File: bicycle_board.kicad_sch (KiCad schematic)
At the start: 57 parts, among them J1 Micro_SD_Card, J10 USB_A, J12 Conn_01x04, J13 Conn_01x04, J2 USB_C_Receptacle_USB2.0_16P, J6 Conn_01x08, J7 Conn_01x05, J8 Conn_01x02, J9 Conn_01x06, Q1 Q_NMOS_GSD, Q2 Q_NMOS_GSD, Q3 Q_NMOS_GSD, Q4 Q_NMOS_GSD, Q5 Q_NMOS_GSD, U13 NS4168, U14 ESP32-C3-WROOM-02U, U15 CH32V203C8T6, U7 74HC595, Y1 12MHz, Y2 32.768kHz

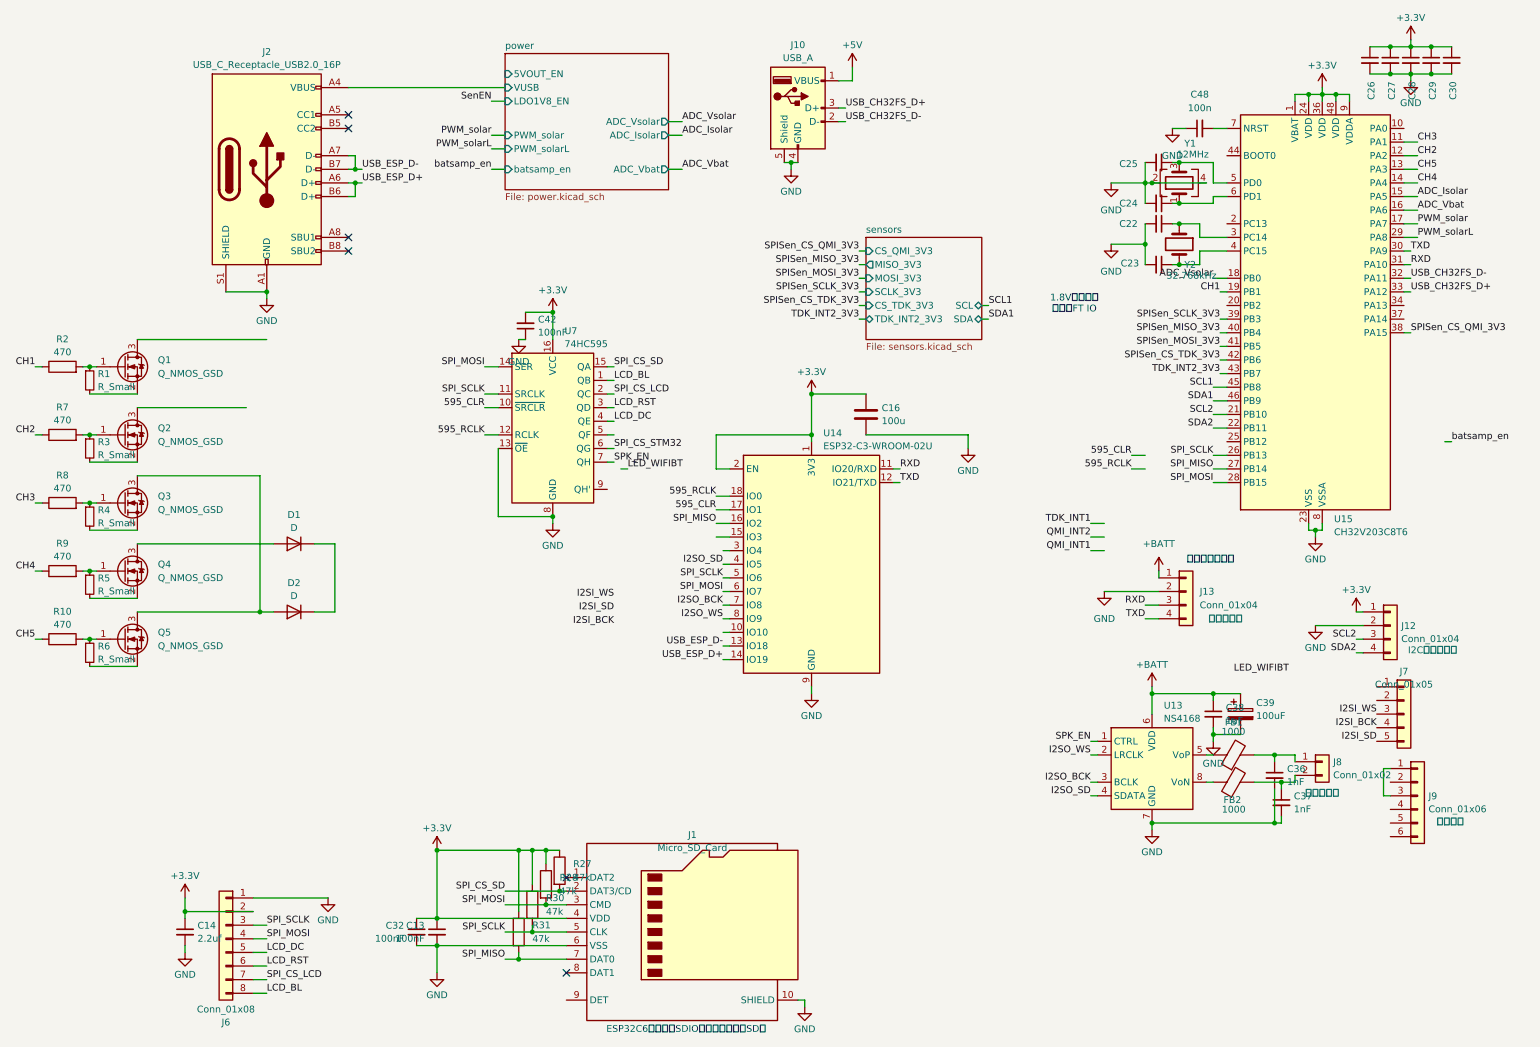
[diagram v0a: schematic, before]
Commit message: 修复一些DRC错误和警告，大多数信号接口改成SH1.0接口
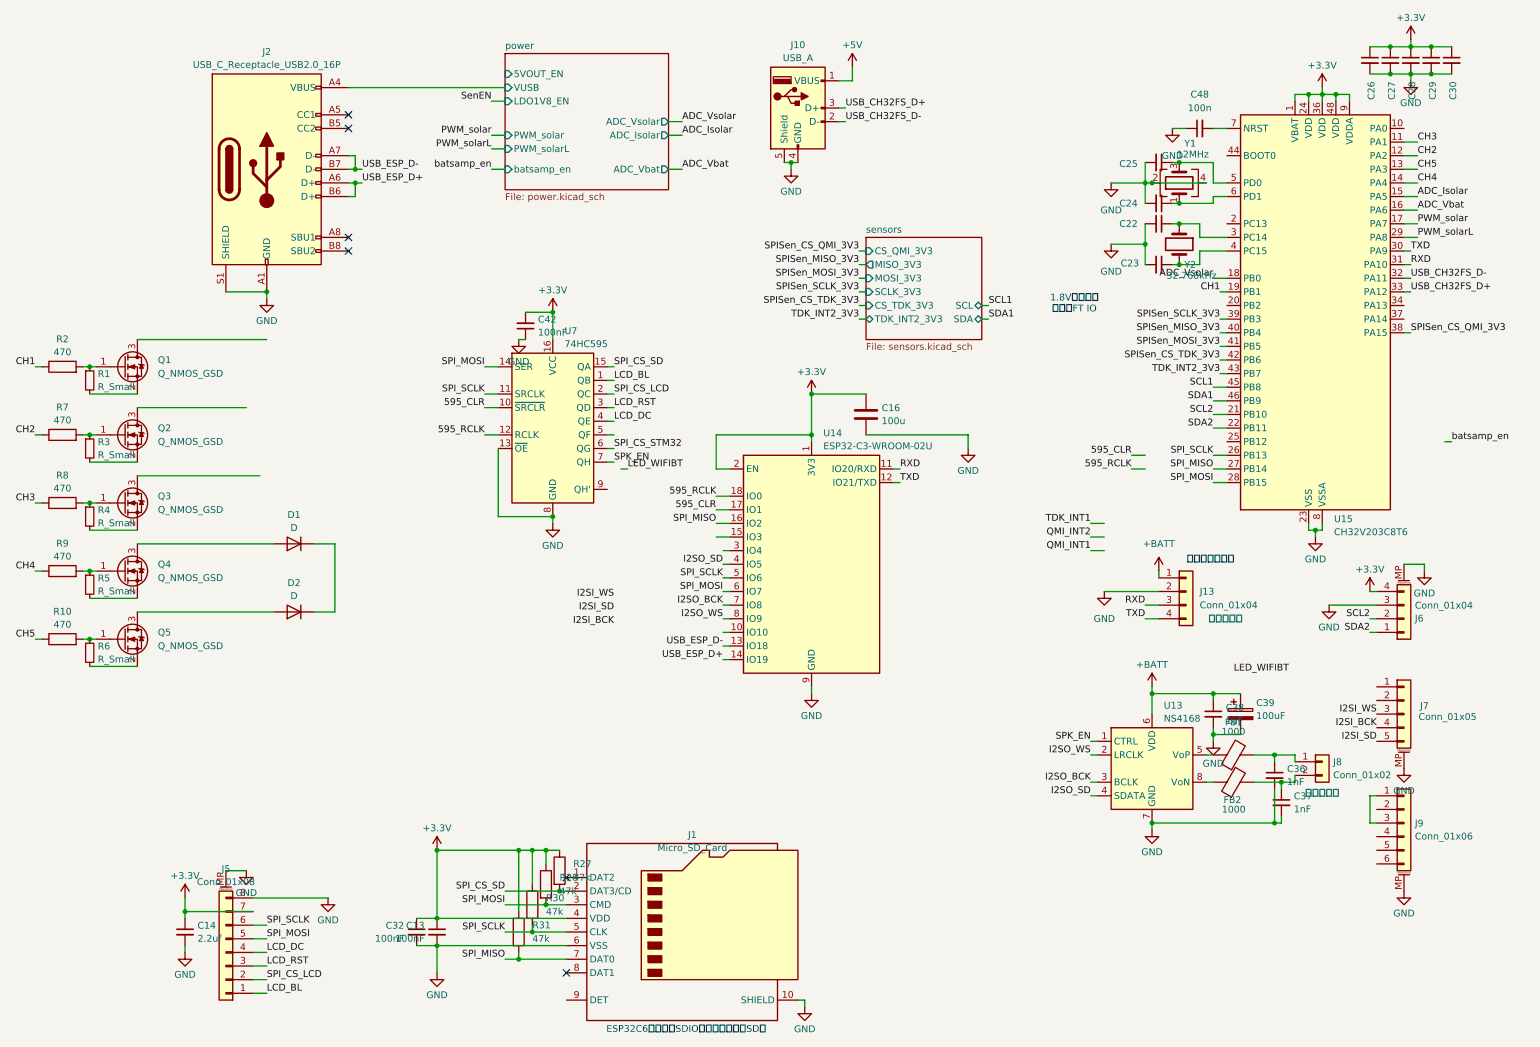
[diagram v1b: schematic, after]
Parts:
- removed J12: Conn_01x04, Connector_JST:JST_GH_BM04B-GHS-TBT_1x04-1MP_P1.25mm_Vertical, symbol Connector_Generic:Conn_01x04
- removed J6: Conn_01x08, Connector_JST:JST_GH_BM08B-GHS-TBT_1x08-1MP_P1.25mm_Vertical, symbol Connector_Generic:Conn_01x08
- added J5: Conn_01x08, Connector_JST:JST_SH_SM08B-SRSS-TB_1x08-1MP_P1.00mm_Horizontal, symbol Connector_Generic_MountingPin:Conn_01x08_MountingPin
- added J6: Conn_01x04, Connector_JST:JST_SH_SM04B-SRSS-TB_1x04-1MP_P1.00mm_Horizontal, symbol Connector_Generic_MountingPin:Conn_01x04_MountingPin
- J7: footprint Connector_JST:JST_GH_BM05B-GHS-TBT_1x05-1MP_P1.25mm_Vertical -> Connector_JST:JST_SH_SM05B-SRSS-TB_1x05-1MP_P1.00mm_Horizontal; symbol Connector_Generic:Conn_01x05 -> Connector_Generic_MountingPin:Conn_01x05_MountingPin
- J9: footprint Connector_JST:JST_SHL_SM06B-SHLS-TF_1x06-1MP_P1.00mm_Horizontal -> Connector_JST:JST_SH_SM06B-SRSS-TB_1x06-1MP_P1.00mm_Horizontal; symbol Connector_Generic:Conn_01x06 -> Connector_Generic_MountingPin:Conn_01x06_MountingPin
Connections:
- net +3.3V: now also J5.7 (Pin_7), J6.4 (Pin_4)
- net GND: now also J7.MP (MountPin), J9.MP (MountPin), J5.8 (Pin_8), J5.MP (MountPin), J6.3 (Pin_3), J6.MP (MountPin)
- net LCD_BL: now also J5.1 (Pin_1)
- net LCD_DC: now also J5.4 (Pin_4)
- net LCD_RST: now also J5.3 (Pin_3)
- net SCL2: now also J6.2 (Pin_2)
- net SDA2: now also J6.1 (Pin_1)
- net SPI_CS_LCD: now also J5.2 (Pin_2)
- net SPI_MOSI: now also J5.5 (Pin_5)
- net SPI_SCLK: now also J5.6 (Pin_6)
- net at D2.2 (A), Q5.3 (D): no longer Q3.3 (D)

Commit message: 添加霍尔元件接口，移除CH2,CH3 MOS通道，调整和连接布线，取消STM32与ESP32的SPI连接
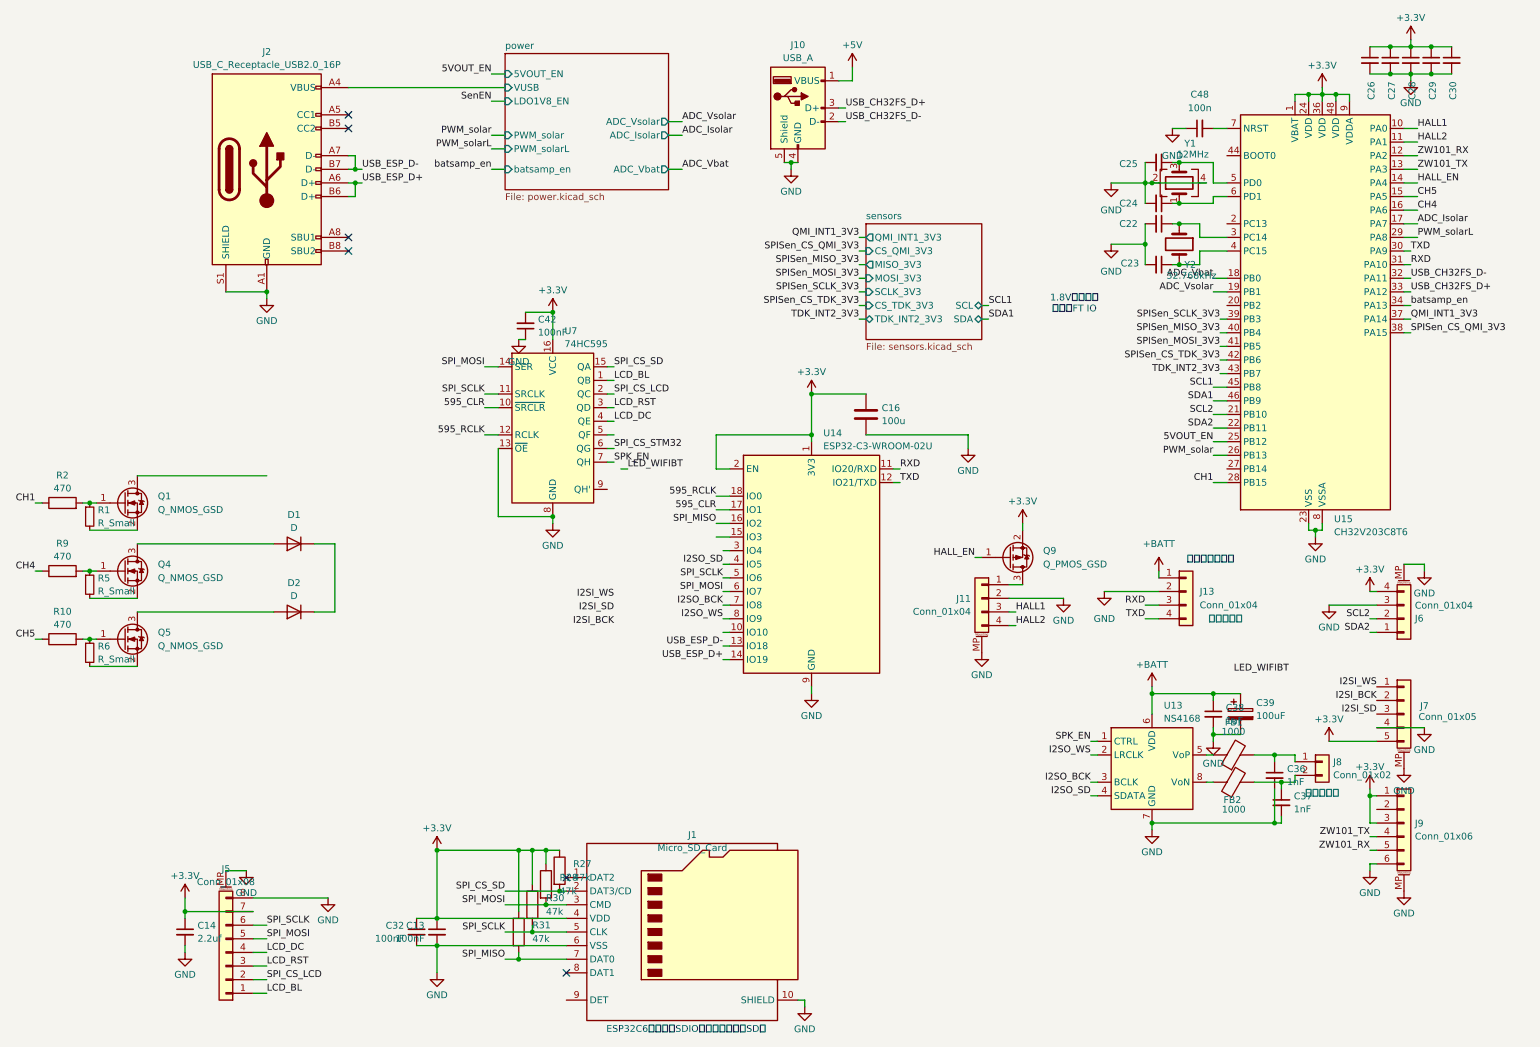
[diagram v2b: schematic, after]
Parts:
- removed Q2, Q3: Q_NMOS_GSD, Package_TO_SOT_SMD:SOT-23, symbol Device:Q_NMOS_GSD
- removed R3, R4: R_Small, Resistor_SMD:R_0402_1005Metric, symbol Device:R_Small
- removed R7, R8: 470, Resistor_SMD:R_0402_1005Metric, symbol Device:R
- added J11: Conn_01x04, Connector_JST:JST_SH_SM04B-SRSS-TB_1x04-1MP_P1.00mm_Horizontal, symbol Connector_Generic_MountingPin:Conn_01x04_MountingPin
- added Q9: Q_PMOS_GSD, Package_TO_SOT_SMD:SOT-523, symbol Device:Q_PMOS_GSD
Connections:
- net CH2 is gone; now on net ZW101_RX: U15.12 (PA2)
- net +3.3V: now also J7.5 (Pin_5), J9.1 (Pin_1), J9.3 (Pin_3), Q9.2 (S)
- net ADC_Isolar: now also U15.17 (PA7); no longer U15.15 (PA5)
- net ADC_Vbat: now also U15.18 (PB0); no longer U15.16 (PA6)
- net ADC_Vsolar: now also U15.19 (PB1); no longer U15.18 (PB0)
- net CH1: now also U15.28 (PB15); no longer U15.19 (PB1)
- net CH4: now also U15.16 (PA6); no longer U15.14 (PA4)
- net CH5: now also U15.15 (PA5); no longer U15.13 (PA3)
- net GND: now also J7.4 (Pin_4), J9.6 (Pin_6), J11.2 (Pin_2), J11.MP (MountPin)
- net I2SI_BCK: now also J7.2 (Pin_2); no longer J7.4 (Pin_4)
- net I2SI_SD: now also J7.3 (Pin_3); no longer J7.5 (Pin_5)
- net I2SI_WS: now also J7.1 (Pin_1); no longer J7.3 (Pin_3)
- net PWM_solar: now also U15.26 (PB13); no longer U15.17 (PA7)
- net SPI_MISO: no longer U15.27 (PB14)
- net SPI_MOSI: no longer U15.28 (PB15)
- net SPI_SCLK: no longer U15.26 (PB13)
- net batsamp_en: now also U15.34 (PA13)
- net HALL1: now reaches U15.10 (PA0)
- net HALL1: now also J11.3 (Pin_3)
- net 5VOUT_EN: now reaches U15.25 (PB12)
- net QMI_INT1_3V3: now reaches U15.37 (PA14)
- net ZW101_TX: now reaches J9.4 (Pin_4)
- net ZW101_TX: now also U15.13 (PA3)
- net ZW101_RX: now reaches J9.5 (Pin_5)
- net CH3 renamed HALL2
- net HALL2: now also J11.4 (Pin_4)
- new net: J11.1 (Pin_1), Q9.3 (D)
- new net HALL_EN: Q9.1 (G), U15.14 (PA4)
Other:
- sheet sensors ports: added QMI_INT1_3V3; removed none
- moved on the sheet: Q1, R1, R2

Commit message: 调整STM32 GPIO使用，移除右侧MOS通道，只在左侧底部保留2个，计划采用PCA9555/TCA9555 GPIO扩展芯片
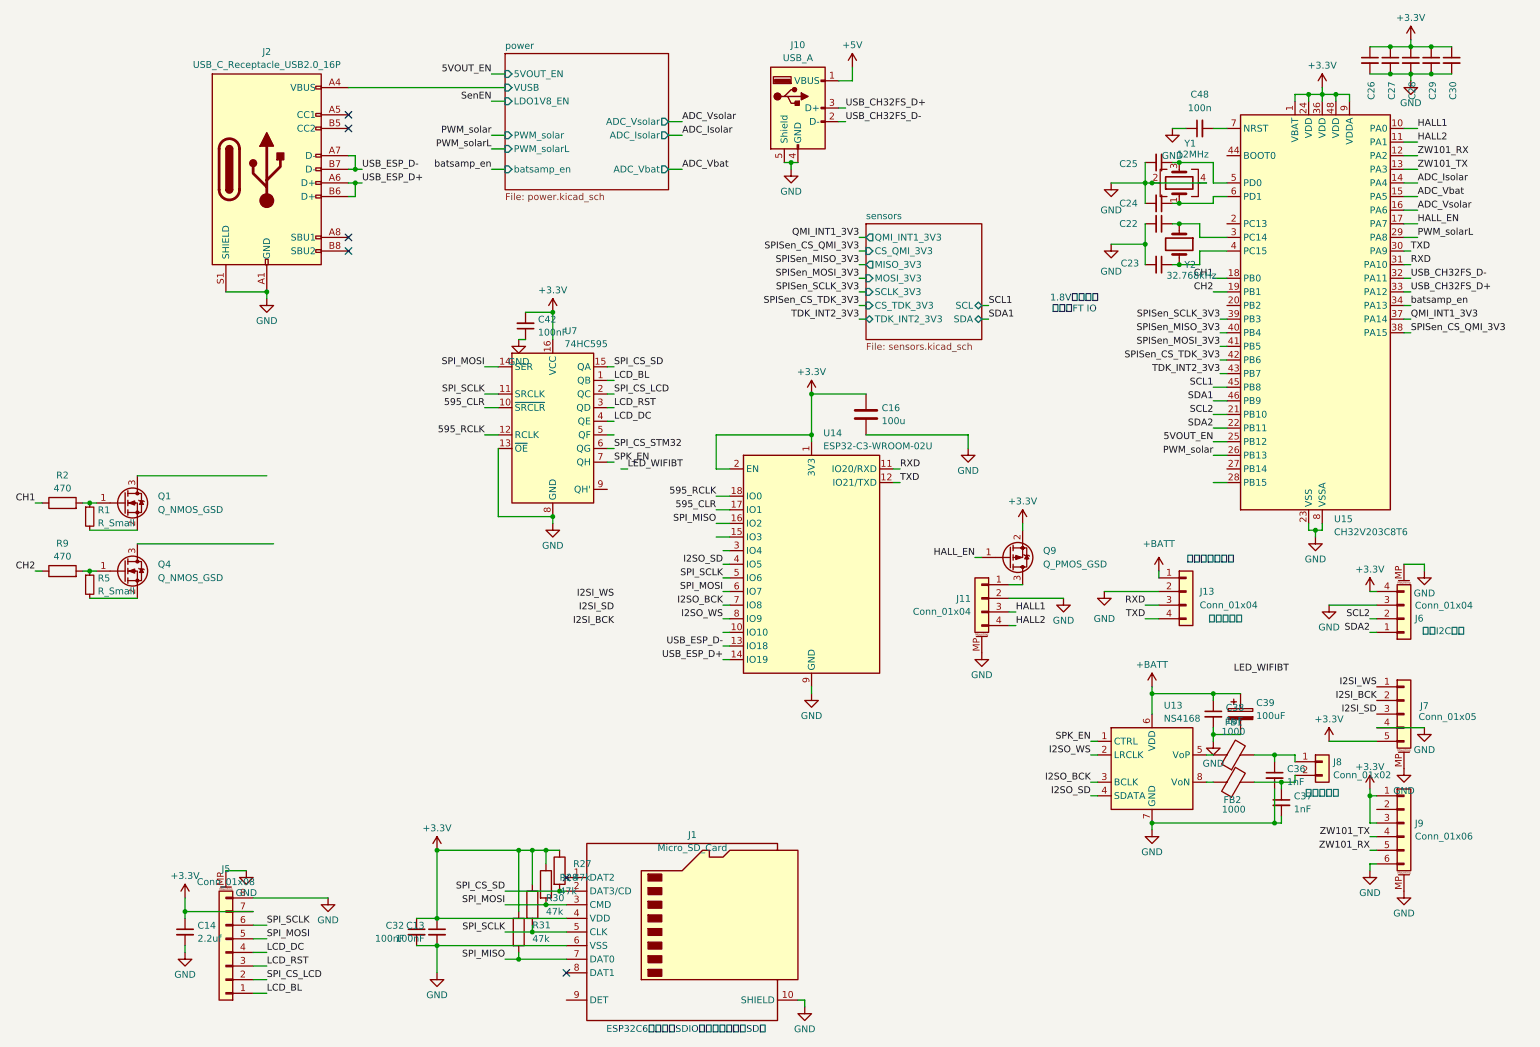
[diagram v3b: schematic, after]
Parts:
- removed D1, D2: D, Diode_SMD:D_SOD-123F, symbol Device:D
- removed Q5: Q_NMOS_GSD, Package_TO_SOT_SMD:SOT-23, symbol Device:Q_NMOS_GSD
- removed R10: 470, Resistor_SMD:R_0402_1005Metric, symbol Device:R
- removed R6: R_Small, Resistor_SMD:R_0402_1005Metric, symbol Device:R_Small
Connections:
- net CH5 is gone; now on net ADC_Vbat: U15.15 (PA5)
- net ADC_Isolar: now also U15.14 (PA4); no longer U15.17 (PA7)
- net ADC_Vbat: no longer U15.18 (PB0)
- net ADC_Vsolar: now also U15.16 (PA6); no longer U15.19 (PB1)
- net CH1: now also U15.18 (PB0); no longer U15.28 (PB15)
- net HALL_EN: now also U15.17 (PA7); no longer U15.14 (PA4)
- net CH4 renamed CH2
- net CH2: now also U15.19 (PB1); no longer U15.16 (PA6)
